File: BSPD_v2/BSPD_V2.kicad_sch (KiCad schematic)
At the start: 25 parts, among them K1 G5V-1, P1 0430450827, T1 T-BJT-NPN, U1 SN74HC00N, U2 LM393P, U3 LM393P, U4 LM393P, U5 SN74HC08N, U6 LM2596T-5

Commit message: update
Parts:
- U1: footprint SN74HC00N:DIP794W45P254L1969H508Q14 -> bspd:SN7432
- U5: footprint SN74HC08N:DIP794W45P254L1969H508Q14 -> bspd:SN7432
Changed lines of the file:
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@@
 			)
 		)
-		(property "Footprint" "SN74HC00N:DIP794W45P254L1969H508Q14"
+		(property "Footprint" "bspd:SN7432"
 			(at 120.65 44.45 0)
 			(effects
@@
 			)
 		)
-		(property "Footprint" "SN74HC08N:DIP794W45P254L1969H508Q14"
+		(property "Footprint" "bspd:SN7432"
 			(at 125.73 92.71 0)
 			(effects

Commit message: updated library
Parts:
- U1, U5: footprint bspd:SN7432 -> PCM_4ms_Package_DIP:DIP-14_W7.62mm
- U4: footprint LM393P:DIP794W45P254L959H508Q8 -> Package_DIP:CERDIP-8_W7.62mm_SideBrazed_LongPads_Socket
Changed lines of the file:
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@@
 	(paper "A4")
 	(junction
-		(at 29.21 138.43)
+		(at 97.79 191.77)
 		(diameter 0)
 		(color 0 0 0 0)
 	)
 	(junction
-		(at 97.79 191.77)
+		(at 30.48 138.43)
 		(diameter 0)
 		(color 0 0 0 0)
@@
 	(wire
 		(pts
-			(xy 29.21 138.43) (xy 29.21 170.18)
-		)
-		(stroke
-			(width 0)
-			(type default)
-		)
-	)
-	(wire
-		(pts
 			(xy 33.02 49.53) (xy 33.02 54.61)
 		)
@@
 	(wire
 		(pts
-			(xy 30.48 170.18) (xy 30.48 175.26)
+			(xy 30.48 138.43) (xy 30.48 175.26)
 		)
 		(stroke
@@
 	(wire
 		(pts
-			(xy 95.25 130.81) (xy 95.25 36.83)
+			(xy 30.48 138.43) (xy 43.18 138.43)
 		)
 		(stroke
@@
 	(wire
 		(pts
-			(xy 149.86 134.62) (xy 182.88 134.62)
+			(xy 95.25 130.81) (xy 95.25 36.83)
 		)
 		(stroke
@@
 	(wire
 		(pts
-			(xy 97.79 179.07) (xy 95.25 179.07)
+			(xy 149.86 134.62) (xy 182.88 134.62)
 		)
 		(stroke
@@
 	(wire
 		(pts
-			(xy 149.86 64.77) (xy 229.87 64.77)
+			(xy 97.79 179.07) (xy 95.25 179.07)
 		)
 		(stroke
@@
 	(wire
 		(pts
-			(xy 29.21 170.18) (xy 30.48 170.18)
+			(xy 149.86 64.77) (xy 229.87 64.77)
 		)
 		(stroke
@@
 	(wire
 		(pts
-			(xy 29.21 138.43) (xy 25.4 138.43)
+			(xy 25.4 138.43) (xy 30.48 138.43)
 		)
 		(stroke
@@
 	(wire
 		(pts
-			(xy 29.21 138.43) (xy 43.18 138.43)
-		)
-		(stroke
-			(width 0)
-			(type default)
-		)
-	)
-	(wire
-		(pts
 			(xy 133.35 173.99) (xy 143.51 173.99)
 		)
@@
 	(global_label "BPS_sensor"
 		(shape input)
-		(at 29.21 147.32 0)
+		(at 30.48 147.32 0)
 		(fields_autoplaced yes)
 		(effects
@@
 		)
 		(property "Intersheetrefs" "${INTERSHEET_REFS}"
-			(at 43.1413 147.32 0)
+			(at 44.4113 147.32 0)
 			(effects
 				(font
@@
 			)
 		)
-		(property "Footprint" "LM393P:DIP794W45P254L959H508Q8"
+		(property "Footprint" "Package_DIP:CERDIP-8_W7.62mm_SideBrazed_LongPads_Socket"
 			(at 132.08 137.16 0)
 			(effects
@@
 			)
 		)
-		(property "Footprint" "bspd:SN7432"
+		(property "Footprint" "PCM_4ms_Package_DIP:DIP-14_W7.62mm"
 			(at 120.65 44.45 0)
 			(effects
@@
 			)
 		)
-		(property "Footprint" "bspd:SN7432"
+		(property "Footprint" "PCM_4ms_Package_DIP:DIP-14_W7.62mm"
 			(at 125.73 92.71 0)
 			(effects

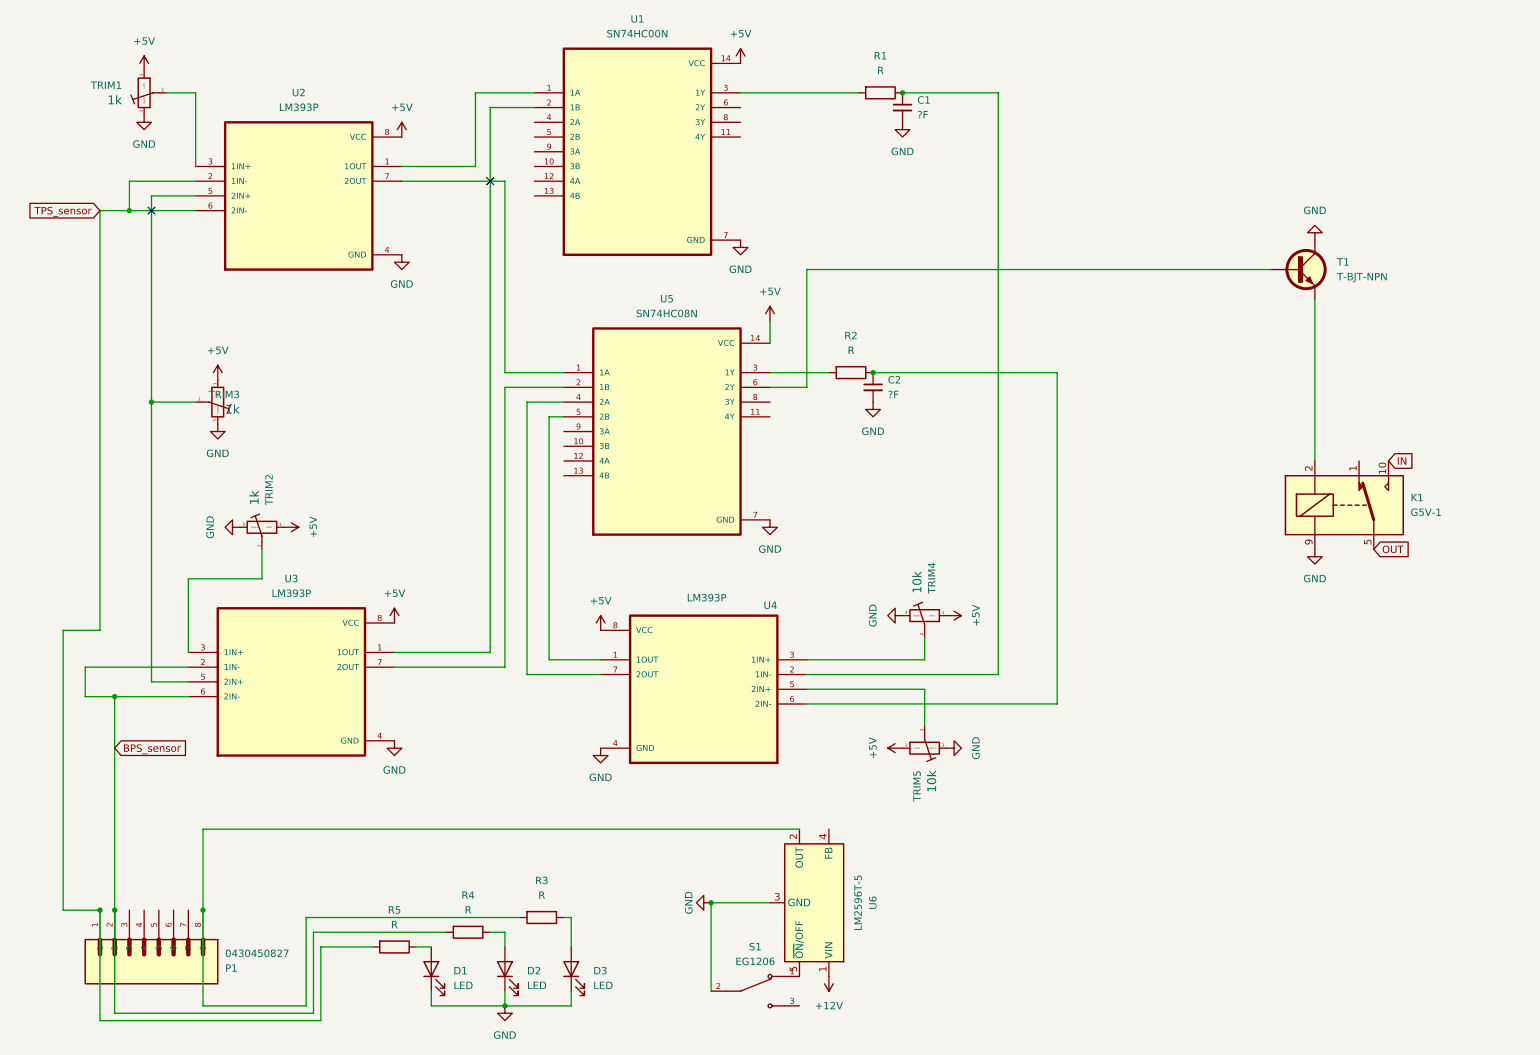
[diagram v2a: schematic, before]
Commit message: pcb design updated using proper footprints and routing
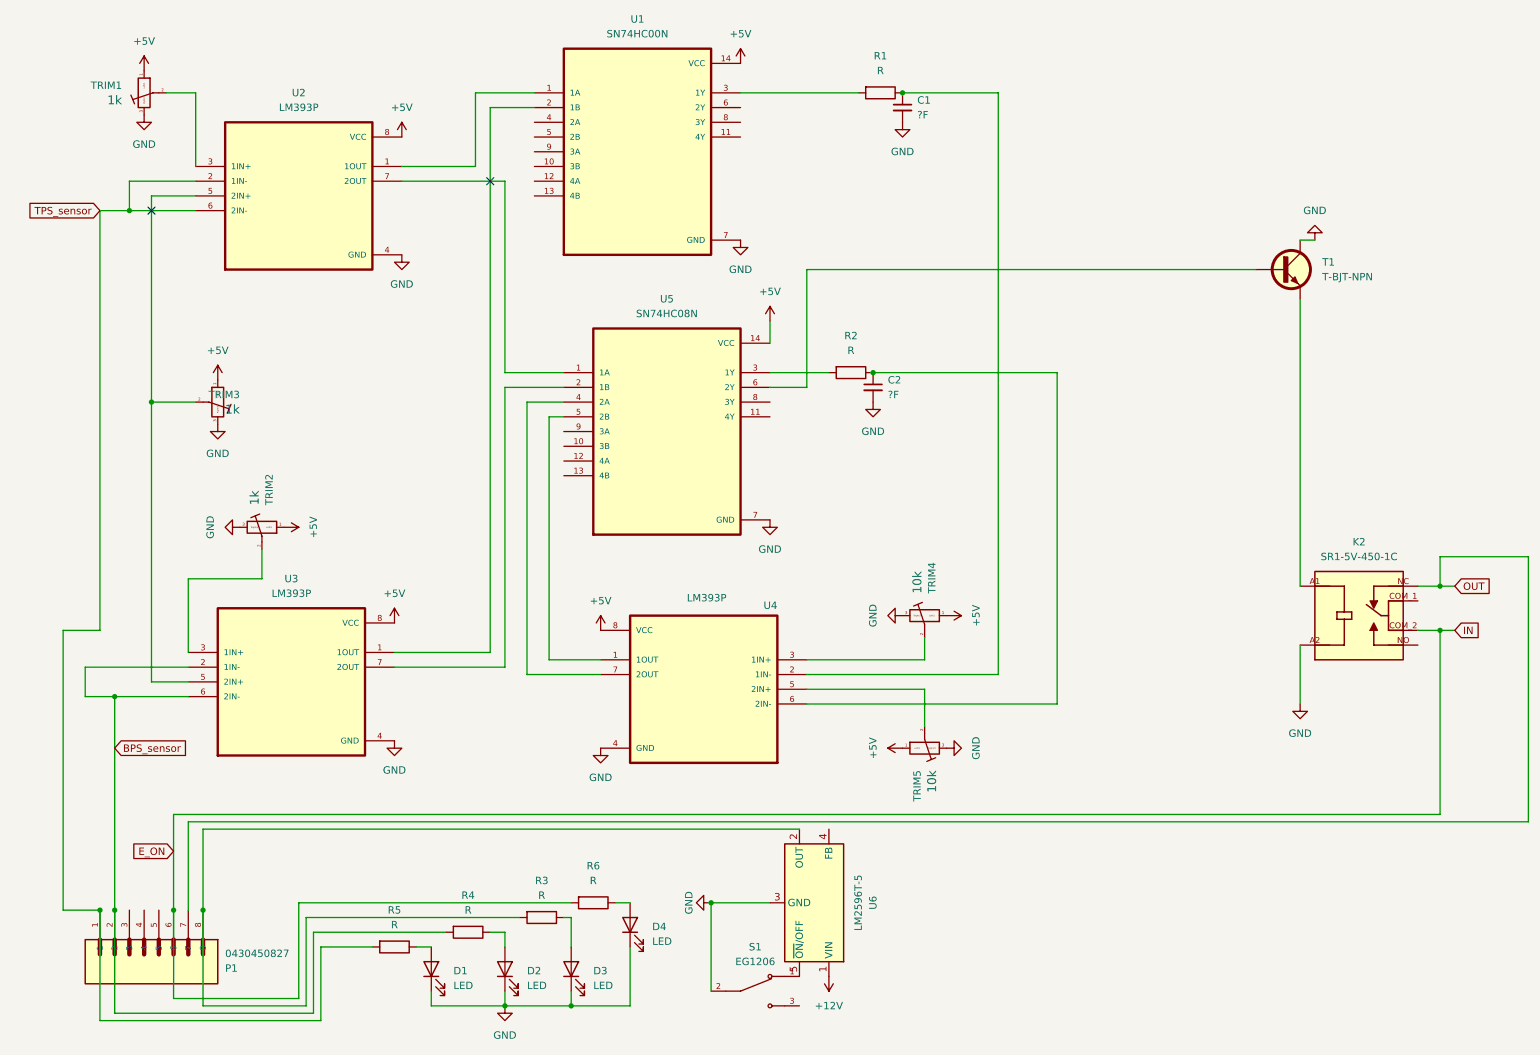
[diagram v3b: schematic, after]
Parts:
- removed K1: G5V-1, Relay_THT:Relay_SPDT_Omron_G5V-1, symbol Relay:G5V-1
- added D4: LED, LED_THT:LED_D5.0mm_Horizontal_O6.35mm_Z9.0mm, symbol Device:LED
- added K2: SR1-5V-450-1C, SR1-5V-450-1C:RELAY_SR1-5V-450-1C, symbol SR1-5V-450-1C_relay_bspd:SR1-5V-450-1C
- added R6: R, PCM_Resistor_THT_AKL:R_Axial_DIN0204_L3.6mm_D1.6mm_P2.54mm_Vertical, symbol Device:R
- R1, R2, R3, R4, R5: footprint PCM_Resistor_THT_AKL:R_Axial_DIN0918_L18.0mm_D9.0mm_P25.40mm_Horizontal -> PCM_Resistor_THT_AKL:R_Axial_DIN0204_L3.6mm_D1.6mm_P2.54mm_Vertical
- U2, U3: footprint LM393P:DIP794W45P254L959H508Q8 -> PCM_4ms_Package_DIP:DIP-8pin_TH
- U4: footprint Package_DIP:CERDIP-8_W7.62mm_SideBrazed_LongPads_Socket -> PCM_Package_DIP_AKL:DIP-8_W7.62mm
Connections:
- net GND: now also D4.1 (K), K2.A2
- net OUT: now also P1.7, K2.NC
- net at T1.3 (E): now also K2.A1
- net E_ON: now reaches P1.6
- net E_ON: now also K2.COM_2, R6.2
- new net: D4.2 (A), R6.1
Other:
- moved on the sheet: T1

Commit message: Added footprints for 5v Regulator
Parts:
- U2, U3: footprint PCM_4ms_Package_DIP:DIP-8pin_TH -> PCM_Package_DIP_AKL:DIP-8_W7.62mm
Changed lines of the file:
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@@
 			)
 		)
-		(property "Footprint" "PCM_4ms_Package_DIP:DIP-8pin_TH"
+		(property "Footprint" "PCM_Package_DIP_AKL:DIP-8_W7.62mm"
 			(at 60.96 135.89 0)
 			(effects
@@
 			)
 		)
-		(property "Footprint" "PCM_4ms_Package_DIP:DIP-8pin_TH"
+		(property "Footprint" "PCM_Package_DIP_AKL:DIP-8_W7.62mm"
 			(at 62.23 52.07 0)
 			(effects

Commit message: Update
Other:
- note added: "BSPD_V2"
- note added: "TEAM PETRONARC"
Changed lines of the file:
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@@
 	(generator_version "9.0")
 	(paper "A4")
+	(rectangle
+		(start 204.47 25.4)
+		(end 262.89 40.64)
+		(stroke
+			(width 0)
+			(type default)
+		)
+		(fill
+			(type none)
+		)
+	)
+	(text "BSPD_V2"
+		(exclude_from_sim no)
+		(at 195.326 173.736 0)
+		(effects
+			(font
+				(size 3 3)
+				(color 170 71 255 0.79)
+			)
+		)
+	)
+	(text "TEAM PETRONARC"
+		(exclude_from_sim no)
+		(at 233.68 32.512 0)
+		(effects
+			(font
+				(face "UbuntuMono Nerd Font")
+				(size 5 5)
+				(color 94 213 255 1)
+			)
+		)
+	)
 	(junction
 		(at 259.08 127)
